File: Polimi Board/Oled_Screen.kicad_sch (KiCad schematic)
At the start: 1 part, among them J1 I2C Oled Screen

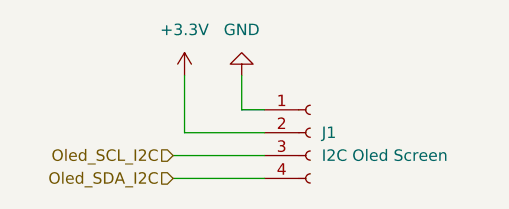
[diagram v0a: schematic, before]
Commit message: Solved issues
3.3V 3V3 and others
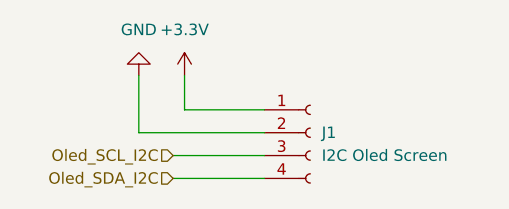
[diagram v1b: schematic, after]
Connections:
- net +3.3V: now also J1.1 (Pin_1); no longer J1.2 (Pin_2)
- net GND: now also J1.2 (Pin_2); no longer J1.1 (Pin_1)
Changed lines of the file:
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@@
 	(wire
 		(pts
-			(xy 121.92 85.09) (xy 121.92 91.44)
-		)
-		(stroke
-			(width 0)
-			(type default)
-		)
-	)
-	(wire
-		(pts
-			(xy 128.27 88.9) (xy 128.27 85.09)
-		)
-		(stroke
-			(width 0)
-			(type default)
-		)
-	)
-	(wire
-		(pts
-			(xy 128.27 88.9) (xy 130.81 88.9)
-		)
-		(stroke
-			(width 0)
-			(type default)
-		)
-	)
-	(wire
-		(pts
-			(xy 121.92 91.44) (xy 130.81 91.44)
+			(xy 121.92 85.09) (xy 121.92 88.9)
+		)
+		(stroke
+			(width 0)
+			(type default)
+		)
+	)
+	(wire
+		(pts
+			(xy 116.84 91.44) (xy 130.81 91.44)
+		)
+		(stroke
+			(width 0)
+			(type default)
+		)
+	)
+	(wire
+		(pts
+			(xy 116.84 85.09) (xy 116.84 91.44)
+		)
+		(stroke
+			(width 0)
+			(type default)
+		)
+	)
+	(wire
+		(pts
+			(xy 121.92 88.9) (xy 130.81 88.9)
 		)
 		(stroke
@@
 	(symbol
 		(lib_id "power:GND")
-		(at 128.27 85.09 180)
+		(at 116.84 85.09 180)
 		(unit 1)
 		(exclude_from_sim no)
@@
 		(fields_autoplaced yes)
 		(property "Reference" "#PWR022"
-			(at 128.27 78.74 0)
+			(at 116.84 78.74 0)
 			(effects
 				(font
@@
 		)
 		(property "Value" "GND"
-			(at 128.27 80.01 0)
+			(at 116.84 80.01 0)
 			(effects
 				(font
@@
 		)
 		(property "Footprint" ""
-			(at 128.27 85.09 0)
+			(at 116.84 85.09 0)
 			(effects
 				(font
@@
 		)
 		(property "Datasheet" ""
-			(at 128.27 85.09 0)
+			(at 116.84 85.09 0)
 			(effects
 				(font
@@
 		)
 		(property "Description" ""
-			(at 128.27 85.09 0)
-			(effects
-				(font
+			(at 116.84 85.09 0)
+			(effects
+				(font
